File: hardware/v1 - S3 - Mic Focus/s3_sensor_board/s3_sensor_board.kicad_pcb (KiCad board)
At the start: 4 copper layers, 76 x 62 mm, 91 parts, among them J101 Conn_01x02, J102 Conn_01x02, J103 Conn_01x02, J104 Conn_01x02, J201 3.3V, J302 Micro_SD_Card_Det, J303 Conn_Coaxial, J304 UART, J305 EXT1, J306 EXT2, J307 I2C, J308 SPI, J309 USB_C_Receptacle_USB2.0_16P, J501 Conn_01x05, J502 Conn_01x05, SW301 BOOT, SW302 RST, U201 LMR36006, U302 ESP32-C3, U401 INA237, U402 INA237, U601 SHT4x, Y301 32kHz RTC Crystal, Y302 40 MHz

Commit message: WIP
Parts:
- removed C207: 20pF, Capacitor_SMD:C_0805_2012Metric
- removed C208, C502, C503, C504, C601: 1uF, Capacitor_SMD:C_0805_2012Metric
- removed C505, C506: DNP, Capacitor_SMD:C_0805_2012Metric
- removed D1: D_Small, Diode_SMD:D_SOD-123
- removed G***: LOGO, BVH_Logos:SkyIron_logo_Back
- removed J103, J104: Conn_01x02, Connector_Phoenix_MSTB:PhoenixContact_MSTBA_2,5_2-G-5,08_1x02_P5.08mm_Horizontal
- removed J201: 3.3V, Connector_PinHeader_2.54mm:PinHeader_1x03_P2.54mm_Vertical
- removed J306: EXT2, Connector_PinHeader_2.54mm:PinHeader_1x03_P2.54mm_Vertical
- removed J307: I2C, Connector_PinHeader_2.54mm:PinHeader_1x04_P2.54mm_Vertical
- removed J308: SPI, Connector_PinHeader_2.54mm:PinHeader_1x06_P2.54mm_Vertical
- removed J309: USB_C_Receptacle_USB2.0_16P, Connector_USB:USB_C_Receptacle_GCT_USB4085
- removed J501, J502: Conn_01x05, Connector_PinHeader_2.54mm:PinHeader_1x05_P2.54mm_Horizontal
- removed JP201: USB Power Jumper, Jumper:SolderJumper-2_P1.3mm_Bridged_RoundedPad1.0x1.5mm
- removed L302: 5.6nH, Inductor_SMD:L_0603_1608Metric
- removed R401, R402: 4mR, Resistor_SMD:R_2512_6332Metric
- removed U303: ~, BVH_Components_Misc:Diode_10Pin_DFN2510A-10_10-XFDFN_SOT1176-1
- removed U402: INA237, Package_SO:VSSOP-10_3x3mm_P0.5mm
- added AE301: ANT, BVH_RF_Ham:ANT2012LL13R2400A, F.Cu at (63.4, 90.2)
- added C316: 10pF, Capacitor_SMD:C_0603_1608Metric, F.Cu at (78.0, 45.3)
- added C317: 10pF, Capacitor_SMD:C_0603_1608Metric, F.Cu at (78.0, 47.8)
- added C403: 1uF, Capacitor_SMD:C_0805_2012Metric, F.Cu at (80.0, 120.0)
- added C404: 1uF, Capacitor_SMD:C_0805_2012Metric, F.Cu at (80.0, 123.0)
- added C405: DNP, Capacitor_SMD:C_0805_2012Metric, F.Cu at (80.0, 126.0)
- added C406: DNP, Capacitor_SMD:C_0805_2012Metric, F.Cu at (80.0, 129.1)
- added FB301: ~, Resistor_SMD:R_0805_2012Metric, F.Cu at (85.4, 63.6)
- added J301: UART, Connector_PinHeader_2.54mm:PinHeader_1x03_P2.54mm_Vertical, F.Cu at (99.5, 50.5)
- added J401: Conn_01x05, Connector_PinHeader_2.54mm:PinHeader_1x05_P2.54mm_Horizontal, F.Cu at (98.1, 116.9)
- added J402: Conn_01x05, Connector_PinHeader_2.54mm:PinHeader_1x05_P2.54mm_Horizontal, F.Cu at (98.6, 101.4)
- added J701: Conn_01x08, Connector_PinHeader_2.54mm:PinHeader_1x08_P2.54mm_Vertical, F.Cu at (130.3, 78.8)
- added JP301: RF Ant Sel, BVH_Components_Misc:Jumper_Resistor_0603_2_Way, F.Cu at (63.0, 87.6)
- added R103: 2k2, Resistor_SMD:R_0603_1608Metric, F.Cu at (115.4, 52.2)
- added R104: 2k2, Resistor_SMD:R_0603_1608Metric, F.Cu at (115.4, 54.8)
- added R204: 10 k, Resistor_SMD:R_0603_1608Metric, F.Cu at (148.6, 77.7)
- added R205: 10 k, Resistor_SMD:R_0603_1608Metric, F.Cu at (152.5, 77.9)
- added R315: 50k, Resistor_SMD:R_0603_1608Metric, F.Cu at (86.0, 42.8)
- added R316: 50k, Resistor_SMD:R_0603_1608Metric, F.Cu at (86.0, 45.3)
- added R317: 50k, Resistor_SMD:R_0603_1608Metric, F.Cu at (86.0, 47.8)
- added R318: 50k, Resistor_SMD:R_0603_1608Metric, F.Cu at (86.0, 50.3)
- added R319: 50k, Resistor_SMD:R_0603_1608Metric, F.Cu at (86.0, 52.8)
- added R320: 0, Resistor_SMD:R_0603_1608Metric, F.Cu at (86.0, 55.3)
- added R321: 0, Resistor_SMD:R_0603_1608Metric, F.Cu at (86.0, 57.8)
- added U602: R, BVH_Audio:Knowles_PDM_SMD_ThroughPort, F.Cu at (199.1, 93.0)
- C201: value 0.1uF -> 22uF; footprint Capacitor_SMD:C_0603_1608Metric -> Capacitor_SMD:C_0805_2012Metric
- C202: value 4.7uF -> 0.1uF; footprint Capacitor_SMD:C_1206_3216Metric -> Capacitor_SMD:C_0603_1608Metric
- C203: value 220nF -> 10pF; footprint Capacitor_SMD:C_1206_3216Metric -> Capacitor_SMD:C_0805_2012Metric
- C204: value 220nF -> 22uF; footprint Capacitor_SMD:C_1206_3216Metric -> Capacitor_SMD:C_0805_2012Metric
- C205: value 15uF -> 22uF; footprint Capacitor_SMD:C_1206_3216Metric -> Capacitor_SMD:C_0805_2012Metric
- C206: value 15uF -> 0.1uF; footprint Capacitor_SMD:C_1206_3216Metric -> Capacitor_SMD:C_0603_1608Metric
- C305: value 10uF -> 0.1uF; footprint Capacitor_SMD:C_0805_2012Metric -> Capacitor_SMD:C_0603_1608Metric
- C306: value 0.1uF -> 10uF; footprint Capacitor_SMD:C_0603_1608Metric -> Capacitor_SMD:C_0805_2012Metric
- C309, C310: value 12.5pF -> DNP
- C311: value 10pF -> 0.1uF
- C312: value 10pF -> 2.1pF
- C314: value 2.1pF -> 12.5pF
- C315: value 0.1uF -> 12.5pF
- C401, C402: value 0.1uF -> 1uF; footprint Capacitor_SMD:C_0603_1608Metric -> Capacitor_SMD:C_0805_2012Metric
- J101: footprint Connector_Phoenix_MSTB:PhoenixContact_MSTBA_2,5_2-G-5,08_1x02_P5.08mm_Horizontal -> Connector_PinHeader_2.54mm:PinHeader_1x02_P2.54mm_Vertical
- J102: value Conn_01x02 -> PWR; footprint Connector_Phoenix_MSTB:PhoenixContact_MSTBA_2,5_2-G-5,08_1x02_P5.08mm_Horizontal -> Connector_PinHeader_2.54mm:PinHeader_1x03_P2.54mm_Vertical
- J302: value Micro_SD_Card_Det -> I2C; footprint BVH_Connectors_Misc:MicroSD_Socket_Unbranded -> Connector_PinHeader_2.54mm:PinHeader_1x04_P2.54mm_Vertical
- J303: value Conn_Coaxial -> USB_C_Receptacle_USB2.0_16P; footprint Connector_Coaxial:U.FL_Molex_MCRF_73412-0110_Vertical -> Connector_USB:USB_C_Receptacle_GCT_USB4085
- J304: value UART -> Conn_Coaxial; footprint Connector_PinHeader_2.54mm:PinHeader_1x03_P2.54mm_Vertical -> Connector_Coaxial:U.FL_Molex_MCRF_73412-0110_Vertical
- J305: value EXT1 -> Micro_SD_Card_Det; footprint Connector_PinHeader_2.54mm:PinHeader_1x03_P2.54mm_Vertical -> BVH_Connectors_Misc:MicroSD_Socket_Unbranded
- L201: value 10uH -> 3.3uH; footprint Inductor_SMD:L_Taiyo-Yuden_MD-4040 -> Inductor_SMD:L_Taiyo-Yuden_MD-2020
- L301: value 2.0nH -> 5.6nH; footprint Inductor_SMD:L_0402_1005Metric -> Inductor_SMD:L_0603_1608Metric
- R101: value 2k2 -> 500k
- R102: value 2k2 -> 100k
- R201: value 100k -> 51.1 k
- R202: value 43.2k -> 45.3 k
- R203: value 100k -> 30 k
- R301: value 100k -> R_Small
- R303, R306: value R_Small -> 100k
- R304, R305: value 0 -> 5.1k
- R309, R310: value 50k -> 0
- R311, R312: value 5.1k -> 50k
- R313: value 33R -> 50k
- R314: value 50k -> 33R
- SW301: footprint BVH_Switches:TacButton_SMD_5mm_5mm -> BVH_Switches:TacButton_SMD_4.0x3.0mm_SPST_NO_2P
- SW302: footprint BVH_Switches:Tac_SMD_6.4mm_Side_SPST_NO -> BVH_Switches:TacButton_SMD_4.0x3.0mm_SPST_NO_2P
- U201: value LMR36006 -> TPS564257DRLR; footprint BVH_Power:LMR36006-VQFN-HR -> Package_TO_SOT_SMD:SOT-563
- U302: value ESP32-C3 -> ESP32-S3; footprint Package_DFN_QFN:QFN-32-1EP_5x5mm_P0.5mm_EP3.45x3.45mm -> Package_DFN_QFN:QFN-56-1EP_7x7mm_P0.4mm_EP4x4mm
- U401: value INA237 -> ~; footprint Package_SO:VSSOP-10_3x3mm_P0.5mm -> Package_SO:SOIC-16_3.9x9.9mm_P1.27mm
- U501: value ~ -> SHT4x; footprint Package_SO:SOIC-16_3.9x9.9mm_P1.27mm -> Sensor_Humidity:Sensirion_DFN-4_1.5x1.5mm_P0.8mm_SHT4x_NoCentralPad
- U601: value SHT4x -> L; footprint Sensor_Humidity:Sensirion_DFN-4_1.5x1.5mm_P0.8mm_SHT4x_NoCentralPad -> BVH_Audio:Knowles_PDM_SMD_ThroughPort
- moved H102 134.0 mm to (34.0, 43.6)
- moved H103 124.9 mm to (34.0, 50.8)
- moved U601 100.4 mm to (195.4, 93.0)
- moved H101 83.5 mm to (34.0, 36.5)
- moved C302 76.7 mm to (74.0, 37.8), turned to 0 degrees
- moved SW302 76.5 mm to (175.3, 111.0), turned to 0 degrees
- moved C304 73.0 mm to (74.0, 42.8)
- moved R306 71.8 mm to (82.0, 42.8), turned to 0 degrees
- moved R304 70.3 mm to (82.0, 37.8), turned to 0 degrees
- moved C313 69.5 mm to (61.0, 45.5), turned to 0 degrees
- moved J302 67.6 mm to (90.3, 38.8), turned to 0 degrees
- moved C315 67.2 mm to (78.0, 42.8), turned to 0 degrees
- moved R102 66.7 mm to (178.3, 81.0), turned to 0 degrees
- moved R101 66.3 mm to (178.3, 78.5), turned to 0 degrees
- moved L301 66.3 mm to (60.7, 51.0)
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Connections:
- C201 pad 1: Net-(U201-BOOT) -> /TPS56425X Regulator/Vin
- C201 pad 2: /Power/SW -> GND
- C202 pad 1: VIN -> /TPS56425X Regulator/Vin
- C203 pad 1: VIN -> +3.3V
- C203 pad 2: GND -> Net-(U201-FB)
- C204 pad 1: VIN -> +3.3V
- C305 pad 1: +3.3V -> /Microprocessor/VDD33A
- C307 pad 1: /Microprocessor/VDD33A -> +3.3V
- C309 pad 1: Net-(C309-Pad1) -> /Microprocessor/USB_N
- C310 pad 1: /Microprocessor/XTAL_32K_N -> /Microprocessor/USB_P
- C311 pad 1: Net-(C311-Pad1) -> GND
- C311 pad 2: GND -> +3.3V
- C312 pad 1: /Microprocessor/XTAL_N -> /Microprocessor/RF
- C313 pad 1: /Microprocessor/RF -> /Microprocessor/RF_ANT
- C314 pad 1: /Microprocessor/RF_ANT -> Net-(C314-Pad1)
- C315 pad 1: GND -> /Microprocessor/XTAL_32K_N
- C315 pad 2: +3.3V -> GND
- C402 pad 1: +3.3V -> /Load Cell Sensor/E_p
- J101 pad 2: /Vbus1_in -> /TPS56425X Regulator/Vin
- J102 pad 1: VIN -> GND
- J102 pad 2: GND -> +3.3V
- J302 pad 1: /Microprocessor/SD_DAT2 -> GND
- J302 pad 2: /Microprocessor/SD_CS -> +3.3V
- J302 pad 3: /Microprocessor/SPI_COPI -> /Load Cell Sensor/SDA
- J302 pad 4: Net-(J302-VDD) -> /Load Cell Sensor/SCK
- J304 pad 1: GND -> Net-(J304-In)
- J304 pad 2: /Microprocessor/UART_RX -> GND
- J305 pad 1: GND -> /Microprocessor/SD_DAT2
- J305 pad 2: VIN -> /Microprocessor/SD_CS
- J305 pad 3: /Microprocessor/EXT_1 -> /Microprocessor/SD_CMD
- L201 pad 1: /Power/SW -> Net-(U201-SW)
- L301 pad 1: +3.3V -> /Microprocessor/RF
- L301 pad 2: /Microprocessor/VDD33A -> /Microprocessor/RF_ANT
- R101 pad 1: +3.3V -> /TPS56425X Regulator/Vin
- R101 pad 2: /Power Measurement/I2C_SCL -> /Microprocessor/Vin_DIV
- R102 pad 1: +3.3V -> /Microprocessor/Vin_DIV
- R102 pad 2: /Power Measurement/I2C_SDA -> GND
- R201 pad 1: +3.3V -> /TPS56425X Regulator/Vin
- R201 pad 2: /Power/FB -> Net-(U201-EN)
- R202 pad 1: /Power/FB -> +3.3V
- R202 pad 2: GND -> Net-(U201-FB)
- R203 pad 1: +3.3V -> Net-(U201-EN)
- R203 pad 2: P_GOOD -> GND
- R301 pad 1: /Microprocessor/GPIO08_BOOT -> Net-(D301-A)
- R301 pad 2: +3.3V -> /Microprocessor/STATUS_LED
- R302 pad 1: /Microprocessor/GPIO02_BOOT -> /Microprocessor/GPIO3_STRAP_PD
- R303 pad 1: /Microprocessor/CHIP_EN -> /Microprocessor/GPIO02_BOOT
- R304 pad 1: /Microprocessor/XTAL_32K_P -> GND
- R304 pad 2: Net-(C309-Pad1) -> Net-(J303-CC1)
- R305 pad 1: /Microprocessor/XTAL_P -> GND
- R305 pad 2: Net-(C311-Pad1) -> Net-(J303-CC2)
- R306 pad 1: Net-(D301-A) -> /Microprocessor/CHIP_EN
- R306 pad 2: /Microprocessor/STATUS_LED -> +3.3V
- R307 pad 1: /Microprocessor/SPI_CIPO -> /Microprocessor/SD_CS
- R308 pad 1: /Microprocessor/SD_CS -> +3.3V
- R308 pad 2: +3.3V -> /Microprocessor/SD_DAT2
- R309 pad 1: /Microprocessor/SPI_SCK -> /Microprocessor/USB_N
- R309 pad 2: +3.3V -> /Microprocessor/USB_uC_N
- R310 pad 1: /Microprocessor/SPI_COPI -> /Microprocessor/USB_P
- R310 pad 2: +3.3V -> /Microprocessor/USB_uC_P
- R311 pad 1: GND -> /Microprocessor/SPI_CIPO
- R311 pad 2: Net-(J309-CC1) -> +3.3V
- R312 pad 1: GND -> /Microprocessor/SPI_COPI
- R312 pad 2: Net-(J309-CC2) -> +3.3V
- R313 pad 1: +3.3V -> /Microprocessor/SPI_SCK
- R313 pad 2: Net-(J302-VDD) -> +3.3V
- R314 pad 2: /Microprocessor/SD_DAT2 -> Net-(J305-VDD)
- U201 pad 1: GND -> /TPS56425X Regulator/Vin
- U201 pad 2: VIN -> Net-(U201-SW)
- U201 pad 3: /Power/SW -> GND
- U201 pad 4: Net-(U201-BOOT) -> /TPS56425X Regulator/PWR_GD
- U201 pad 5: /Power/VCC -> Net-(U201-EN)
- U201 pad 6: GND -> Net-(U201-FB)
- U302 pad 10: /Power Measurement/I2C_SCL -> unconnected-(U302-GPIO5-Pad10)
- U302 pad 11: +3.3V -> unconnected-(U302-GPIO6-Pad11)
- U302 pad 12: /Microprocessor/STATUS_LED -> unconnected-(U302-GPIO7-Pad12)
- U302 pad 13: /Load Cell Sensor/DRDY_NAU -> unconnected-(U302-GPIO8-Pad13)
- U302 pad 14: /Microprocessor/GPIO08_BOOT -> unconnected-(U302-GPIO9-Pad14)
- U302 pad 15: /Microprocessor/GPIO09_BOOT -> /Microprocessor/PDM_CLK
- U302 pad 16: /Microprocessor/EXT_2 -> /Microprocessor/PDM_D0
- U302 pad 17: +3.3V -> /Microprocessor/PDM_D1
- U302 pad 18: /Microprocessor/SD_DET -> /Microprocessor/PDM_D2
- U302 pad 19: unconnected-(U302-SPIHD/GPIO12-Pad19) -> /Microprocessor/PDM_D3
- U302 pad 2: /Microprocessor/VDD33A -> +3.3V
- U302 pad 20: /Microprocessor/SPI_CS1 -> +3.3V
- U302 pad 21: /Microprocessor/SD_CS -> /Microprocessor/XTAL_32K_P
- U302 pad 22: /Microprocessor/SPI_SCK -> /Microprocessor/XTAL_32K_N
- U302 pad 23: /Microprocessor/SPI_COPI -> /Load Cell Sensor/SDA
- U302 pad 24: /Microprocessor/SPI_CIPO -> /Load Cell Sensor/SCK
- U302 pad 25: /Microprocessor/USB_N -> /Microprocessor/USB_uC_N
- U302 pad 26: /Microprocessor/USB_P -> /Microprocessor/USB_uC_P
- U302 pad 27: /Microprocessor/UART_RX -> unconnected-(U302-GPIO21-Pad27)
- U302 pad 28: /Microprocessor/UART_TX -> unconnected-(U302-SPICS1-Pad28)
- U302 pad 29: /Microprocessor/XTAL_N -> unconnected-(U302-VDD_SPI-Pad29)
- U302 pad 3: /Microprocessor/VDD33A -> +3.3V
- U302 pad 30: /Microprocessor/XTAL_P -> unconnected-(U302-SPIHD-Pad30)
- U302 pad 31: +3.3V -> unconnected-(U302-SPIWP-Pad31)
- U302 pad 32: +3.3V -> unconnected-(U302-SPICS0-Pad32)
- U302 pad 33: GND -> unconnected-(U302-SPICLK-Pad33)
- U302 pad 4: /Microprocessor/XTAL_32K_P -> /Microprocessor/CHIP_EN
- U302 pad 5: /Microprocessor/XTAL_32K_N -> /Microprocessor/BOOT_MODE
- U302 pad 6: /Microprocessor/GPIO02_BOOT -> /Microprocessor/Vin_DIV
- U302 pad 7: /Microprocessor/CHIP_EN -> unconnected-(U302-GPIO2-Pad7)
- U302 pad 8: /Microprocessor/EXT_1 -> /Microprocessor/GPIO3_STRAP_PD
- U302 pad 9: /Power Measurement/I2C_SDA -> unconnected-(U302-GPIO4-Pad9)
- U401 pad 1: +3.3V -> /Load Cell Sensor/E_p
- U401 pad 10: /Vbus1_in -> unconnected-(U401-XIN-Pad10)
- U401 pad 2: /Power Measurement/I2C_SDA -> /Load Cell Sensor/S1_N
- U401 pad 3: unconnected-(U401-~{Alert}-Pad3) -> /Load Cell Sensor/S1_P
- U401 pad 4: /Power Measurement/I2C_SDA -> /Load Cell Sensor/S2_N
- U401 pad 5: /Power Measurement/I2C_SCL -> /Load Cell Sensor/S2_P
- U401 pad 6: +3.3V -> Net-(U401-VBG)
- U401 pad 8: /Vbus1_in -> GND
- U401 pad 9: VIN -> GND
- U501 pad 1: /Load Cell Sensor/E_p -> /Load Cell Sensor/SDA
- U501 pad 2: /Load Cell Sensor/S1_N -> /Load Cell Sensor/SCK
- U501 pad 3: /Load Cell Sensor/S1_P -> +3.3V
- U501 pad 4: /Load Cell Sensor/S2_N -> GND
- U601 pad 1: /Power Measurement/I2C_SDA -> /Microprocessor/PDM_D0
- U601 pad 2: /Power Measurement/I2C_SCL -> GND
- U601 pad 3: +3.3V -> GND
- U601 pad 4: GND -> /Microprocessor/PDM_CLK
- Y301 pad 1: Net-(C309-Pad1) -> Net-(C314-Pad1)
- Y302 pad 1: Net-(C311-Pad1) -> Net-(C316-Pad1)
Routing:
- net GND: track 132.2 -> 0.00 mm, vias 69 -> 0
- net /Power Measurement/I2C_SDA: track 120.8 -> 0.00 mm, vias 2 -> 0
- net /Power Measurement/I2C_SCL: track 115.3 -> 0.00 mm, vias 5 -> 0
- net VIN: track 65.3 -> 0.00 mm, vias 16 -> 0
- net +3.3V: track 75.7 -> 12.7 mm, vias 30 -> 0
- net /Microprocessor/CHIP_EN: track 51.3 -> 0.00 mm, vias 2 -> 0
- net /Microprocessor/SPI_COPI: track 42.6 -> 0.00 mm, vias 4 -> 0
- net /Microprocessor/SPI_CIPO: track 42.5 -> 0.00 mm, vias 2 -> 0
- net /Load Cell Sensor/DRDY_NAU: track 36.5 -> 0.00 mm, vias 2 -> 0
- net /Microprocessor/SPI_SCK: track 36.1 -> 0.00 mm, vias 2 -> 0
- net /Load Cell Sensor/E_p: track 32.8 -> 0.00 mm
- net /Microprocessor/SD_DET: track 31.8 -> 0.00 mm, vias 2 -> 0
- net /Microprocessor/EXT_1: track 31.3 -> 0.00 mm, vias 1 -> 0
- net P_GOOD: track 29.7 -> 0.00 mm, vias 2 -> 0
- net /Microprocessor/SPI_CS1: track 29.2 -> 0.00 mm, vias 1 -> 0
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- added copper zone on F.Cu, net /TPS56425X Regulator/Vin
- added copper zone on In2.Cu, net GND
- removed copper zone on In2.Cu, net +3.3V
- removed copper zone on F.Cu, net /Power/SW
- removed copper zone on F.Cu, net /Vbus1_in
- removed copper zone on B.Cu, net GND
- removed copper zone on B.Cu, net VIN
- removed copper zone on F.Cu, net VIN
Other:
- board size 76 x 62 mm -> 20 x 100 mm
- board text removed: "+5V - 60V"
- board text removed: "3.3"
- board text removed: "3.3V"
- board text removed: "A: 0x44"
- board text removed: "AB4EN"
- board text removed: "B: 0x45"
- board text removed: "BOOT G2"
- board text removed: "CIPO"
- board text removed: "COPI"
- board text removed: "CS1 GPIO14"
- board text removed: "E+/RD"
- board text removed: "E-/BK"
- board text removed: "ESP32-C3FH4 sensor board v0.4 Prototype - 2025-Jan-11"
- board text removed: "EXT1 GPIO03 ADC"
- board text removed: "EXT2 GPIO04"
- board text removed: "GND"
- board text removed: "GND/Y"
- board text removed: "J101/102 Board & Sense U401 - 0x46"
- board text removed: "J103/104 Sense Only U401 - 0x47"
- board text removed: "LOAD"
- board text removed: "Load Cell"
- board text removed: "NAU7802 0x2A"
- board text removed: "PGD"
- board text removed: "RX - G20"
- board text removed: "S+/GN"
- board text removed: "S-/WT"
- board text removed: "SCK"
- board text removed: "SCL - G5"
- board text removed: "SD DET - G11 CS - G14 SCK - G15 COPI - G16 CIPO - G17"
- board text removed: "SD PU"
- board text removed: "SDA - G4"
- board text removed: "SHT4X I2C T RH"
- board text removed: "SRC"
- board text removed: "TX - G21"
- board text removed: "VIN"

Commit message: WIP
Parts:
- removed C406: DNP, Capacitor_SMD:C_0805_2012Metric
- removed J402: Conn_01x05, Connector_PinHeader_2.54mm:PinHeader_1x05_P2.54mm_Horizontal
- removed the R307 at (147.5, 133.0)
- removed the R308 at (82.0, 47.8)
- removed the R311 at (135.7, 141.5)
- removed the R312 at (135.7, 144.0)
- removed the R313 at (152.5, 133.0)
- added D101: D USB, Diode_SMD:D_SOD-123, F.Cu at (145.7, 72.6)
- R309: renamed from R314; value 33R -> 0R
- moved C313 127.2 mm to (166.1, 117.1), turned to 180 degrees
- moved L301 123.6 mm to (166.1, 115.5)
- moved C312 118.9 mm to (166.1, 113.9)
- moved J304 116.0 mm to (165.1, 125.1), turned to 180 degrees
- moved R311 111.0 mm to (151.7, 134.8), turned to -90 degrees
- moved R310 110.1 mm to (146.5, 134.8), turned to 90 degrees
- moved R313 109.0 mm to (154.9, 134.8), turned to 90 degrees
- moved AE301 108.4 mm to (167.3, 121.3), turned to -90 degrees
- moved JP301 107.0 mm to (165.3, 118.7), turned to -90 degrees
- moved R314 106.0 mm to (153.3, 134.8), turned to 90 degrees
- moved R312 105.0 mm to (144.9, 134.8), turned to 90 degrees
- moved C310 92.1 mm to (157.9, 90.8)
- moved C309 90.3 mm to (154.7, 90.8), turned to 180 degrees
- moved R307 86.0 mm to (156.1, 94.0)
- moved R308 84.0 mm to (156.1, 92.4), turned to 180 degrees
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- renumbered R302 to R301, R303 to R302, R301 to R303, R309 to R307, R310 to R308, R315 to R310, R316 to R311, R317 to R312, R318 to R313, R319 to R314, R320 to R315, R321 to R316
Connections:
- net Net-(C314-Pad1) renamed /Microprocessor/XTAL_32K_P_R
- net Net-(C316-Pad1) renamed /Microprocessor/XTAL_P_R
- net Net-(J305-VDD) renamed /Microprocessor/SD_VDD
- J305 pad 2: /Microprocessor/SD_CS -> /Microprocessor/SD_DAT3
- U302 pad 14: unconnected-(U302-GPIO9-Pad14) -> /Microprocessor/GPIO09_BOOT
- U302 pad 23: /Load Cell Sensor/SDA -> unconnected-(U302-GPIO17-Pad23)
- U302 pad 24: /Load Cell Sensor/SCK -> unconnected-(U302-GPIO18-Pad24)
- U302 pad 27: unconnected-(U302-GPIO21-Pad27) -> /Load Cell Sensor/DRDY_NAU
- U302 pad 38: /Microprocessor/SD_DAT1 -> unconnected-(U302-GPIO33-Pad38)
- U302 pad 39: /Microprocessor/SD_DAT0 -> unconnected-(U302-GPIO34-Pad39)
- U302 pad 40: /Microprocessor/SD_SCK -> unconnected-(U302-GPIO35-Pad40)
- U302 pad 41: /Microprocessor/SD_CMD -> unconnected-(U302-GPIO36-Pad41)
- U302 pad 42: /Microprocessor/SD_DAT3 -> /Load Cell Sensor/SCK
- U302 pad 43: /Microprocessor/SD_DAT2 -> /Load Cell Sensor/SDA
- U302 pad 44: /Microprocessor/SD_DET -> unconnected-(U302-GPIO39/MTCK-Pad44)
- U302 pad 45: unconnected-(U302-GPIO40/MTDO-Pad45) -> /Microprocessor/SD_DAT1
- U302 pad 47: unconnected-(U302-GPIO41/MTDI-Pad47) -> /Microprocessor/SD_DAT0
- U302 pad 48: unconnected-(U302-GPIO42/MTMS-Pad48) -> /Microprocessor/SD_SCK
- U302 pad 49: /Microprocessor/UART_TX -> /Microprocessor/SD_CMD
- U302 pad 50: /Microprocessor/UART_RX -> /Microprocessor/SD_DAT3
- U302 pad 51: /Microprocessor/STATUS_LED -> /Microprocessor/SD_DAT2
- U302 pad 52: unconnected-(U302-GPIO46-Pad52) -> /Microprocessor/SD_DET
- U302 pad 57: unconnected-(U302-GND-Pad57) -> GND
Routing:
- net /Microprocessor/USB_N: track 0.00 -> 35.9 mm
- net /Microprocessor/USB_P: track 0.00 -> 29.8 mm
- net /Microprocessor/USB_uC_P: track 0.00 -> 11.9 mm
- net /Microprocessor/USB_uC_N: track 0.00 -> 11.6 mm
- net Net-(J303-CC2): track 0.00 -> 10.4 mm
- net /Microprocessor/V_usb: track 0.00 -> 6.74 mm
- net /Microprocessor/XTAL_32K_P_R: track 0.00 -> 4.50 mm
- net /Microprocessor/XTAL_P_R: track 0.00 -> 3.79 mm
- net GND: track 0.00 -> 3.20 mm, vias 0 -> 1
- net /Microprocessor/XTAL_32K_N: track 0.00 -> 3.10 mm
- net /Microprocessor/SD_DAT2: track 0.00 -> 2.28 mm
- net /Microprocessor/SD_DAT1: track 0.00 -> 2.11 mm
- net /Microprocessor/SD_DAT3: track 0.00 -> 2.07 mm
- net /Microprocessor/SD_DAT0: track 0.00 -> 1.91 mm
- net /Microprocessor/SD_CMD: track 0.00 -> 1.86 mm
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
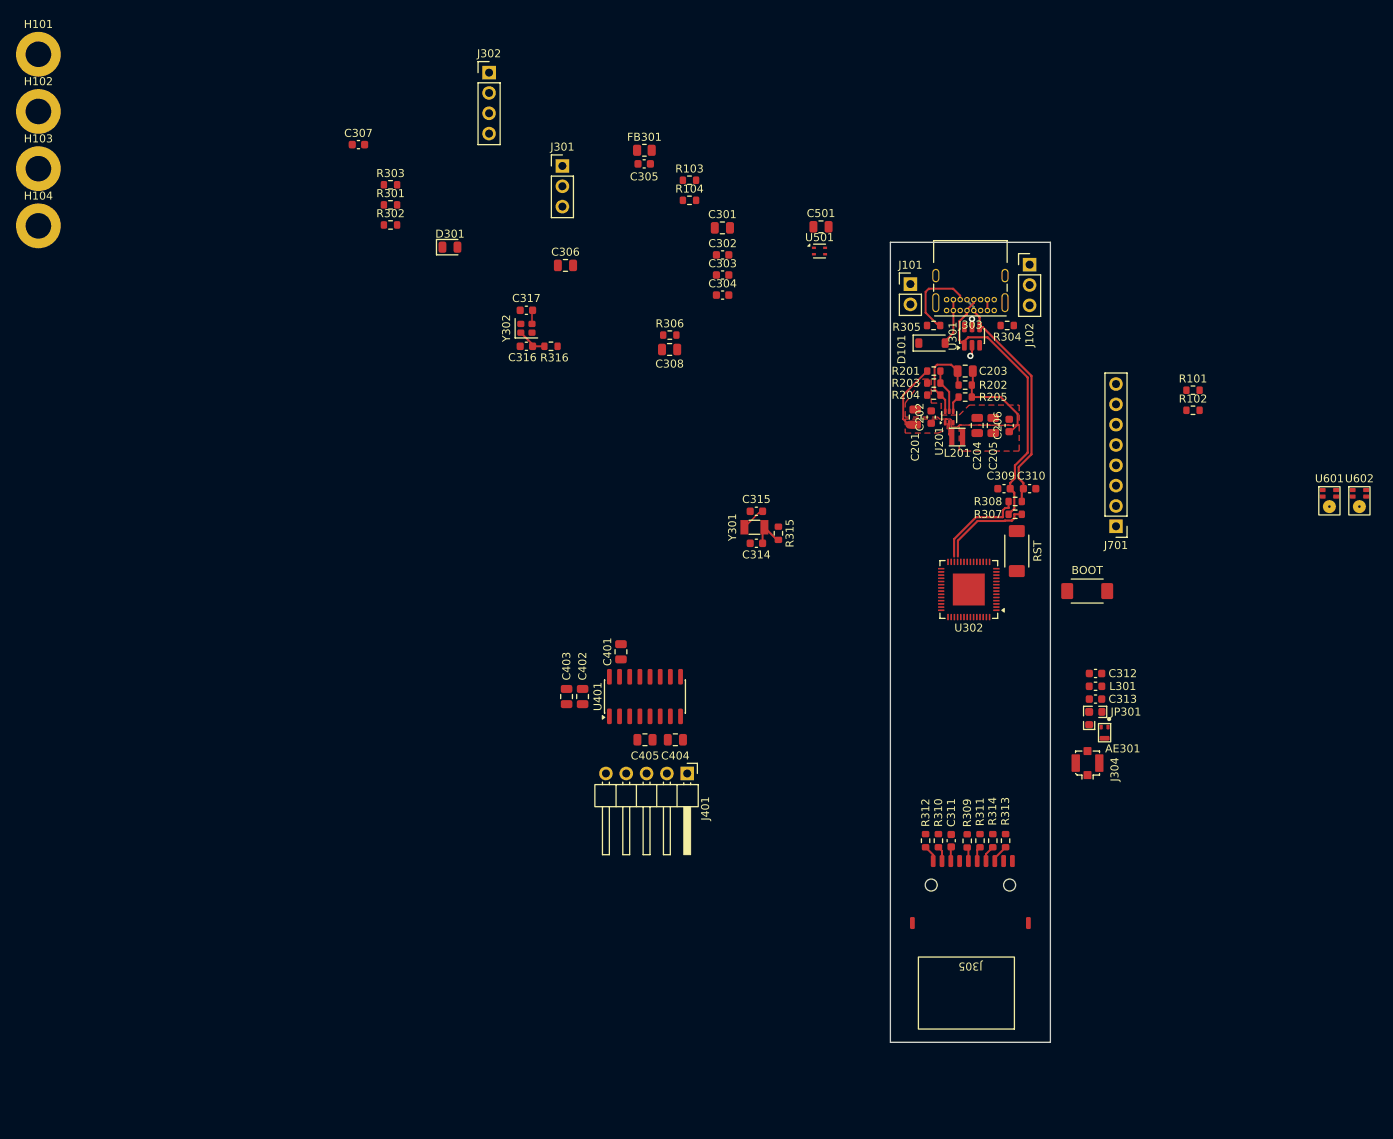
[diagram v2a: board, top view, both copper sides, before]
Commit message: Processor placement and routing work
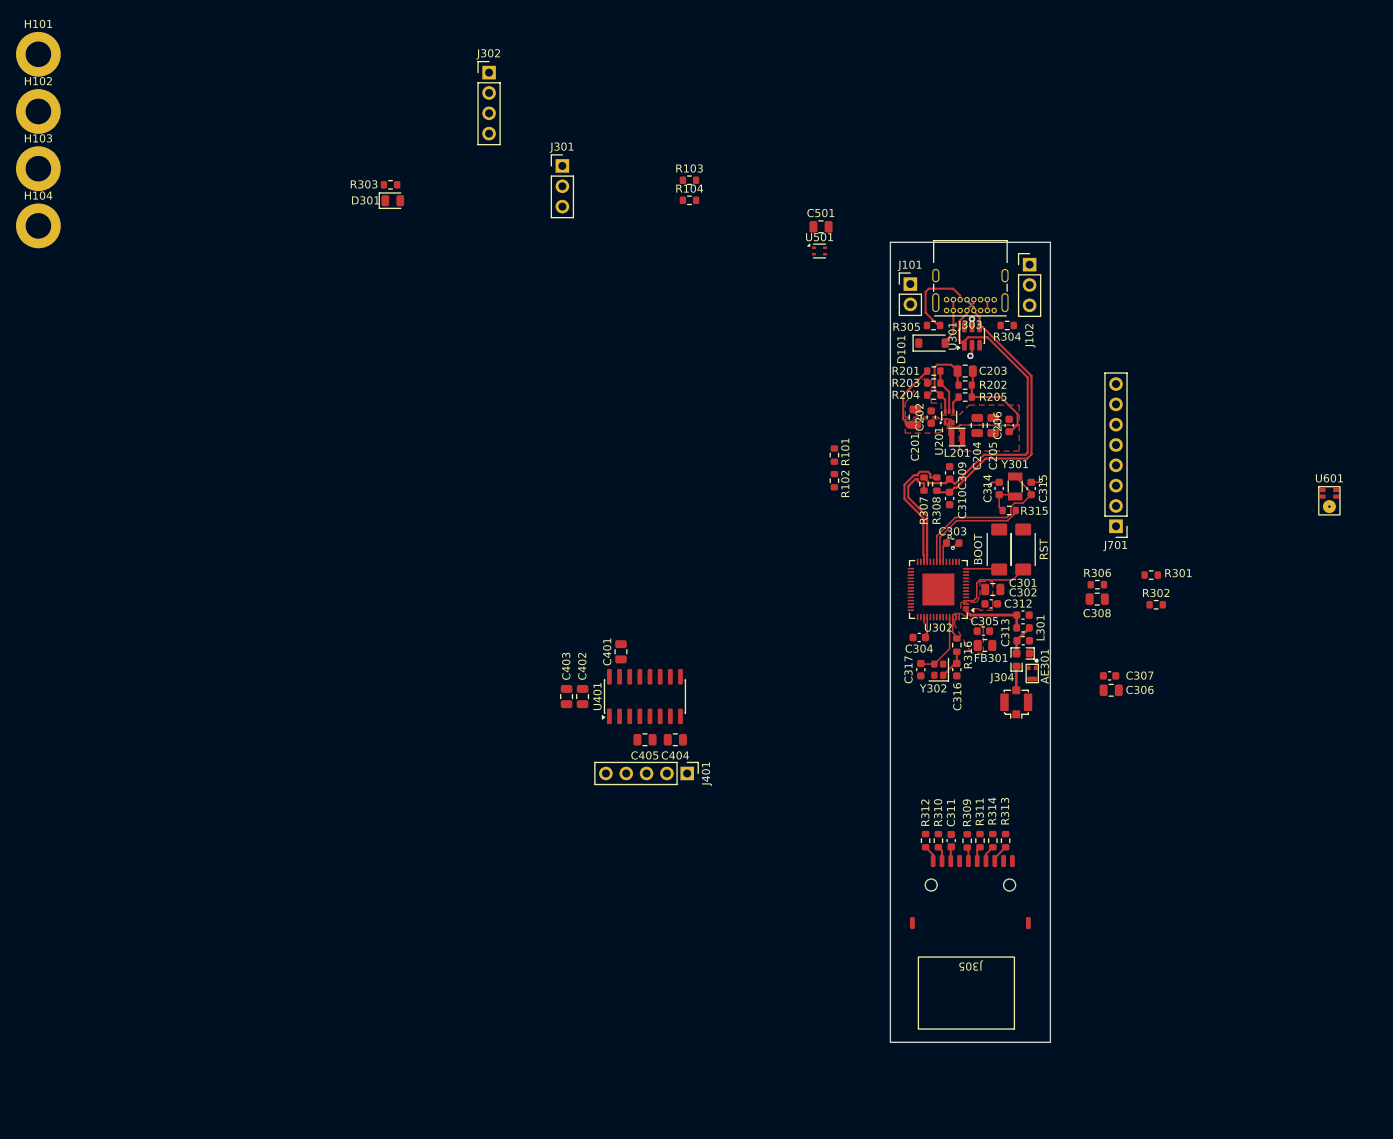
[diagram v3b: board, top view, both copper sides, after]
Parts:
- removed U602: R, BVH_Audio:Knowles_PDM_SMD_ThroughPort
- J401: footprint Connector_PinHeader_2.54mm:PinHeader_1x05_P2.54mm_Horizontal -> Connector_PinHeader_2.54mm:PinHeader_1x05_P2.54mm_Vertical
- moved C307 115.0 mm to (167.9, 114.2)
- moved R302 106.8 mm to (173.7, 105.3)
- moved R301 105.7 mm to (173.1, 101.6)
- moved C306 86.4 mm to (168.1, 116.0)
- moved FB301 75.1 mm to (152.3, 110.4)
- moved C305 72.2 mm to (152.1, 108.6)
- moved C316 67.3 mm to (148.8, 113.4), turned to -90 degrees
- moved Y302 66.9 mm to (146.6, 113.4), turned to 90 degrees
- moved C317 66.7 mm to (144.3, 113.4), turned to -90 degrees
- moved R316 63.0 mm to (148.8, 110.3), turned to -90 degrees
- moved R306 61.9 mm to (166.4, 102.8)
- moved C308 61.9 mm to (166.3, 104.6)
- moved C301 56.4 mm to (153.3, 103.4)
- moved C302 55.0 mm to (153.1, 105.2)
- moved C304 49.4 mm to (144.1, 109.4), turned to 180 degrees
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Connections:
- U302 pad 27: /Load Cell Sensor/DRDY_NAU -> unconnected-(U302-GPIO21-Pad27)
- U302 pad 44: unconnected-(U302-GPIO39/MTCK-Pad44) -> /Load Cell Sensor/DRDY_NAU
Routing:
- net /Microprocessor/XTAL_32K_N: track 3.10 -> 20.8 mm
- net /Microprocessor/XTAL_32K_P: track 0.00 -> 14.1 mm
- net /Microprocessor/CHIP_EN: track 0.00 -> 9.82 mm
- net /Microprocessor/RF: track 0.00 -> 8.17 mm
- net /Microprocessor/USB_P: track 29.8 -> 36.8 mm
- net /Microprocessor/XTAL_N: track 1.73 -> 8.39 mm
- net /Microprocessor/USB_N: track 35.9 -> 42.2 mm
- net +3.3V: track 13.7 -> 19.9 mm, vias 1 -> 2
- net /Microprocessor/GPIO09_BOOT: track 0.00 -> 4.19 mm
- net /Microprocessor/USB_uC_P: track 11.9 -> 16.0 mm
- net /Microprocessor/RF_ANT: track 0.00 -> 3.86 mm
- net GND: track 3.20 -> 6.87 mm, vias 1 -> 4
- net Net-(J304-In): track 0.00 -> 3.02 mm
- net /Microprocessor/XTAL_P: track 0.00 -> 2.88 mm
- net /Microprocessor/USB_uC_N: track 11.6 -> 14.1 mm
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- added copper zone on F.Cu, net /Microprocessor/VDD33A

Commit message: WIP
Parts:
- J701: footprint Connector_PinHeader_2.54mm:PinHeader_1x08_P2.54mm_Vertical -> Connector_IDC:IDC-Header_2x04_P2.54mm_Vertical
- moved SW301 35.6 mm to (184.1, 117.5)
- moved SW302 35.6 mm to (187.1, 117.5)
- moved J701 35.3 mm to (179.1, 129.2), turned to -90 degrees
- moved U501 0.57 mm to (131.9, 61.6)
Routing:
- net /Microprocessor/CHIP_EN: track 9.82 -> 0.00 mm
- net /Microprocessor/GPIO09_BOOT: track 4.19 -> 0.14 mm

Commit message: WIP
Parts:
- added C601: 0.1uF, Capacitor_SMD:C_0603_1608Metric, F.Cu at (152.5, 134.7)
- J305, J701: moved to B.Cu
- R303: value R_Small -> 1k
- moved U601 62.0 mm to (150.3, 135.6)
- moved J701 32.6 mm to (146.7, 125.8)
- moved R309 11.2 mm to (150.1, 146.1)
- moved C311 11.2 mm to (148.1, 146.0)
- moved J305 11.2 mm to (150.5, 149.1), turned to 0 degrees
- moved R310 11.2 mm to (146.5, 146.0)
- moved R311 11.2 mm to (151.7, 146.0)
- moved R312 11.2 mm to (144.9, 146.0)
- moved R313 11.2 mm to (154.9, 146.0)
- moved R314 11.2 mm to (153.3, 146.0)
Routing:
- net GND: track 6.87 -> 10.7 mm
- net +3.3V: track 19.9 -> 21.3 mm
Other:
- board size 20 x 100 mm -> 20 x 110 mm

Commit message: WIP
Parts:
- removed C401, C402, C403, C404: 1uF, Capacitor_SMD:C_0805_2012Metric
- removed C405: DNP, Capacitor_SMD:C_0805_2012Metric
- removed C601: 0.1uF, Capacitor_SMD:C_0603_1608Metric
- removed J401: Conn_01x05, Connector_PinHeader_2.54mm:PinHeader_1x05_P2.54mm_Vertical
- removed J701: Conn_01x08, Connector_IDC:IDC-Header_2x04_P2.54mm_Vertical
- removed U401: ~, Package_SO:SOIC-16_3.9x9.9mm_P1.27mm
- removed U601: L, BVH_Audio:Knowles_PDM_SMD_ThroughPort
- added J103: EXP, Connector_IDC:IDC-Header_2x05_P2.54mm_Vertical, F.Cu at (132.4, 124.8)
- H101, H102, H103, H104: footprint MountingHole:MountingHole_3.2mm_M3_DIN965_Pad -> MountingHole:MountingHole_2.2mm_M2_DIN965_Pad
- moved R312 11.1 mm to (155.9, 144.7), turned to -90 degrees
- moved J305 9.92 mm to (150.4, 139.2)
- moved R313 9.10 mm to (145.9, 144.7), turned to -90 degrees
- moved R310 7.92 mm to (154.3, 144.7), turned to -90 degrees
- moved R314 5.96 mm to (147.5, 144.7), turned to -90 degrees
- moved C311 4.80 mm to (152.7, 144.7), turned to -90 degrees
- moved R311 2.94 mm to (149.1, 144.7), turned to 90 degrees
- moved R309 1.55 mm to (150.7, 144.6), turned to 90 degrees
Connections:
- net /Load Cell Sensor/SCK renamed /I2C_SCL
- net /Load Cell Sensor/SDA renamed /I2C_SDA
- U302 pad 15: /Microprocessor/PDM_CLK -> /PDM_CLK
- U302 pad 16: /Microprocessor/PDM_D0 -> /PDM_D0
- U302 pad 17: /Microprocessor/PDM_D1 -> /PDM_D1
- U302 pad 18: /Microprocessor/PDM_D2 -> /PDM_D2
- U302 pad 19: /Microprocessor/PDM_D3 -> /PDM_D3
- U302 pad 44: /Load Cell Sensor/DRDY_NAU -> /INT
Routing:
- net GND: track 10.7 -> 4.90 mm
- net /Microprocessor/SD_DAT1: track 2.86 -> 0.00 mm
- net /Microprocessor/SD_DAT2: track 2.28 -> 0.00 mm
- net /Microprocessor/SD_DAT3: track 2.07 -> 0.00 mm
- net +3.3V: track 21.3 -> 19.3 mm
- net /Microprocessor/SD_DAT0: track 1.91 -> 0.00 mm
- net /Microprocessor/SD_CMD: track 1.86 -> 0.00 mm
- net /Microprocessor/SD_VDD: track 1.76 -> 0.00 mm
- net /Microprocessor/USB_N: track 42.2 -> 41.5 mm
- net /Microprocessor/USB_P: track 36.8 -> 36.3 mm
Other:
- board size 20 x 110 mm -> 20 x 100 mm
